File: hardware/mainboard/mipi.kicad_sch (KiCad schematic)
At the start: 41 parts

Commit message: More stuff
Signed-off-by: David Shah <dave@ds0.me>
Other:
- moved on the sheet: C?, FB?, U?J, U?K

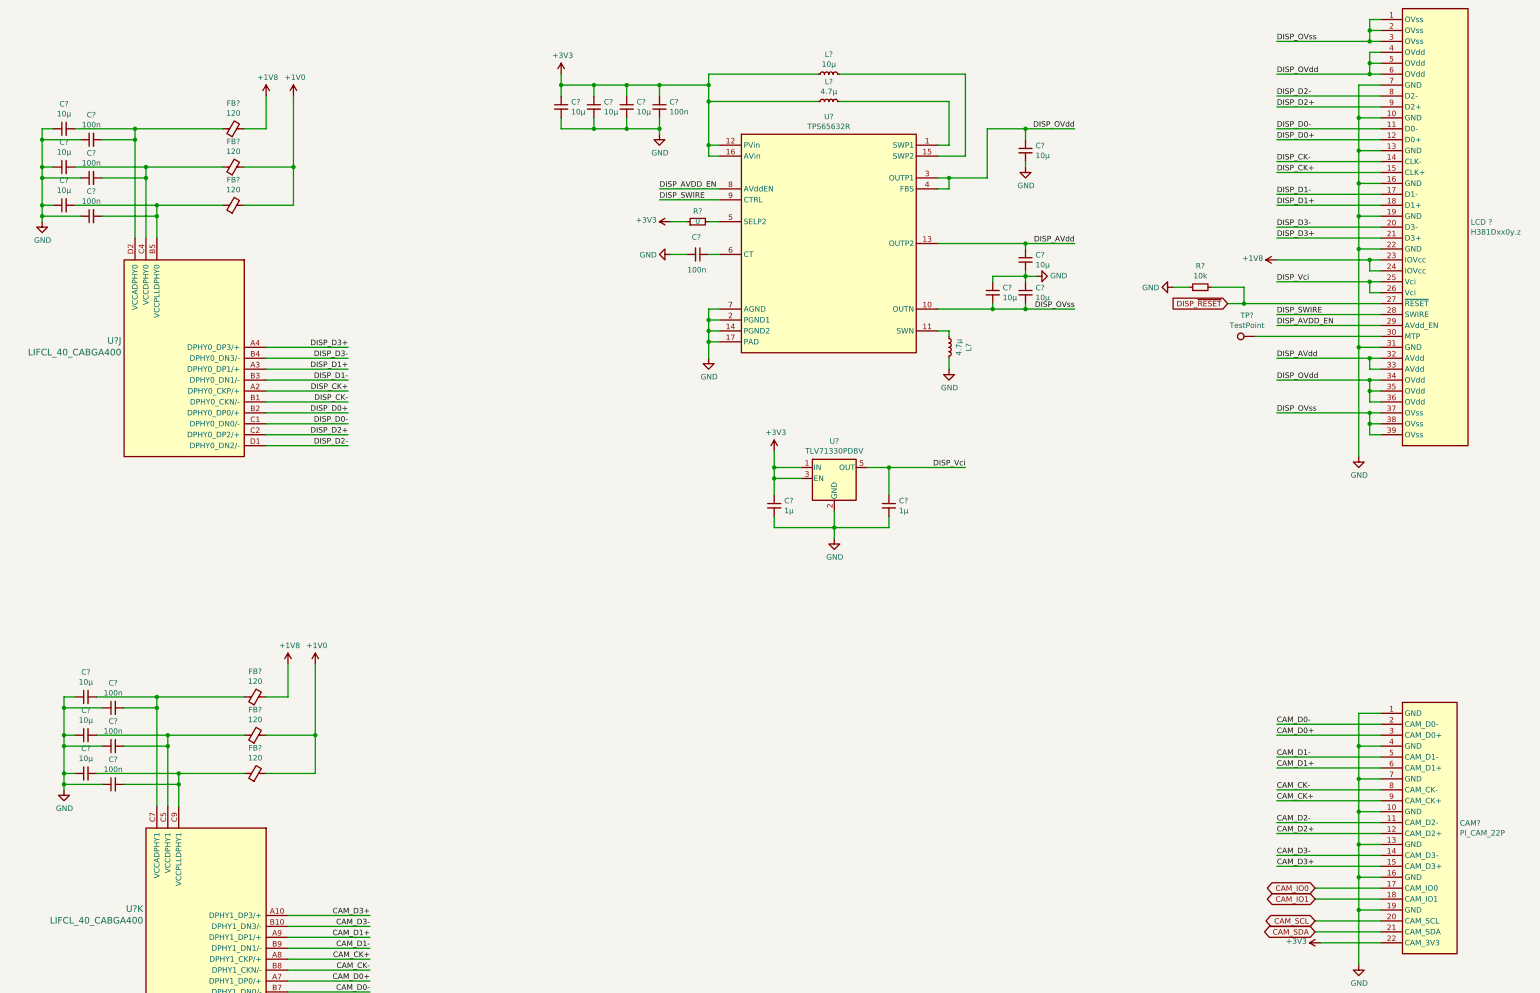
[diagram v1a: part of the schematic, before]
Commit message: Annotate and assign some footpints
Signed-off-by: David Shah <dave@ds0.me>
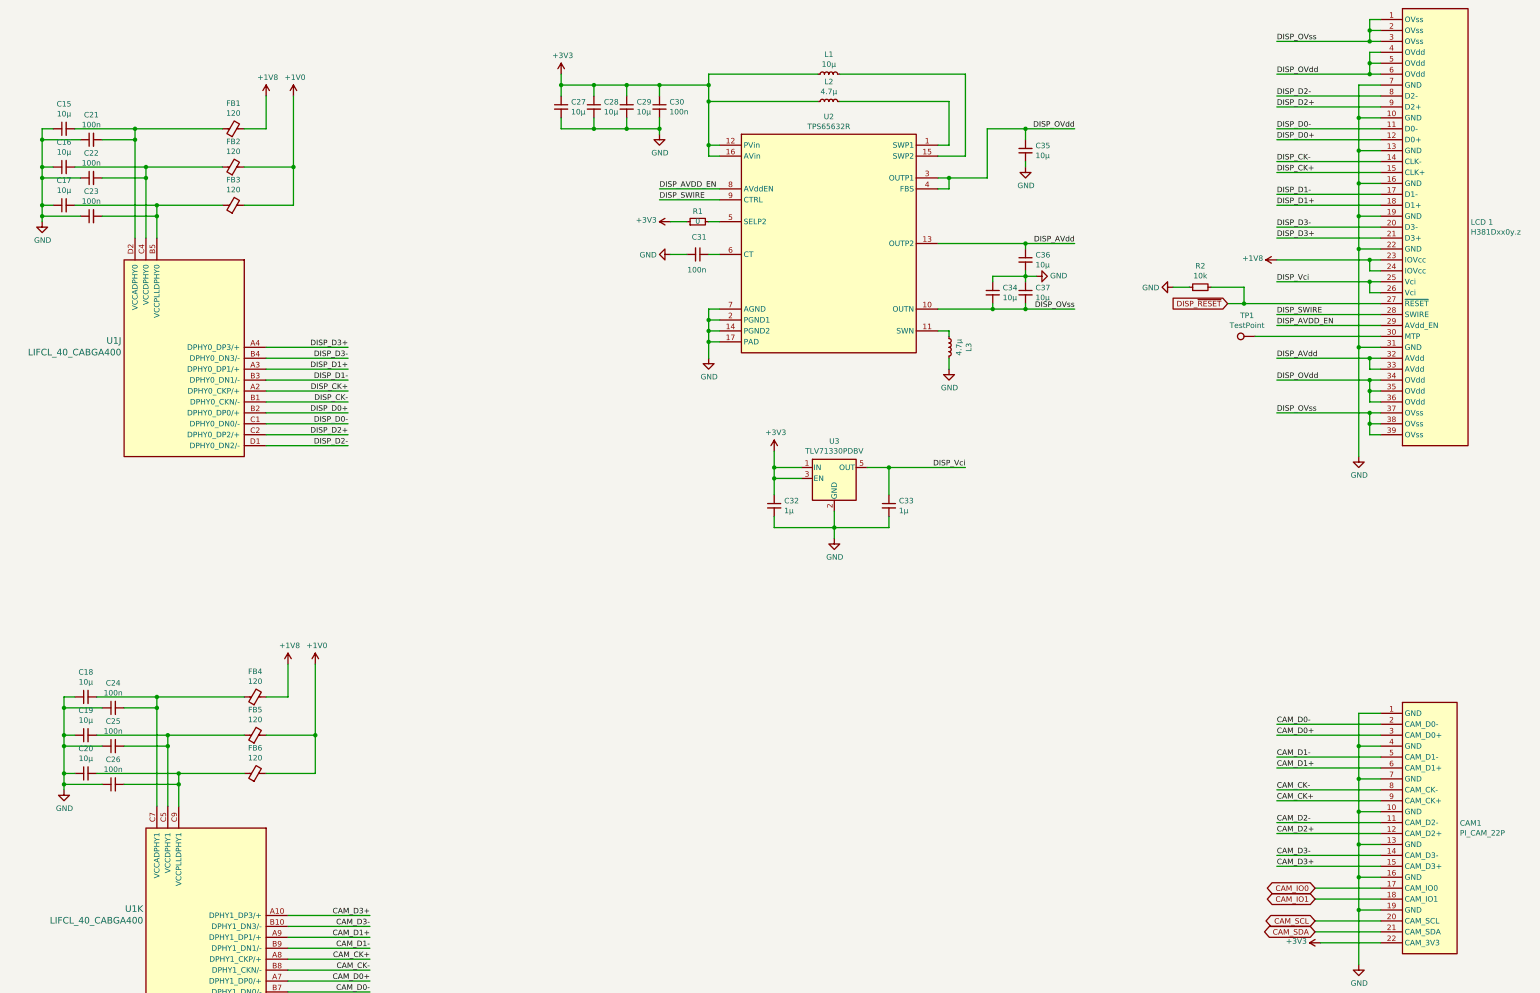
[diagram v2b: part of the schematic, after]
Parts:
- C15, C16, C17, C18, C19, C20, C27, C28, C29, C34, C35, C36, C37: renamed from C?; footprint (none) -> Capacitor_SMD:C_0805_2012Metric
- C21, C22, C23, C24, C25, C26, C30, C31: renamed from C?; footprint (none) -> Capacitor_SMD:C_0402_1005Metric
- C32, C33: renamed from C?; footprint (none) -> Capacitor_SMD:C_0603_1608Metric
- FB1, FB2, FB3, FB4, FB5, FB6: renamed from FB?; footprint (none) -> Inductor_SMD:L_0603_1608Metric
- LCD 1: renamed from LCD ?
- R1, R2: renamed from R?; footprint (none) -> Resistor_SMD:R_0402_1005Metric
- U2: renamed from U?; footprint (none) -> Package_DFN_QFN:QFN-16-1EP_3x3mm_P0.5mm_EP1.7x1.7mm
- gave numbers to parts that had none: 7

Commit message: Add and assign more footprints
Signed-off-by: David Shah <dave@ds0.me>
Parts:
- CAM1: footprint (none) -> meowality:54548-2271
- L1: value 10µ -> XFL3012-103MEB; footprint (none) -> meowality:XFL3012
- L2, L3: value 4.7µ -> XFL4020-472MEB; footprint (none) -> Inductor_SMD:L_Coilcraft_XxL4020
- LCD 1: footprint (none) -> meowality:FH35C-39S-0.3SHW
- TP1: footprint (none) -> TestPoint:TestPoint_Pad_D2.0mm
- U1: footprint (none) -> meowality:BGA-400_20x20_17.0x17.0mm
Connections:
- net GND: now also CAM1.M, LCD 1.M
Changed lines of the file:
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@@
   (junction (at 361.95 224.79) (diameter 1.016) (color 0 0 0 0))
   (junction (at 361.95 232.41) (diameter 1.016) (color 0 0 0 0))
+  (junction (at 361.95 242.57) (diameter 1.016) (color 0 0 0 0))
   (junction (at 364.49 27.94) (diameter 1.016) (color 0 0 0 0))
   (junction (at 364.49 30.48) (diameter 1.016) (color 0 0 0 0))
@@
     (stroke (width 0) (type solid) (color 0 0 0 0))
   )
-  (wire (pts (xy 361.95 232.41) (xy 361.95 245.11))
+  (wire (pts (xy 361.95 232.41) (xy 361.95 242.57))
     (stroke (width 0) (type solid) (color 0 0 0 0))
   )
@@
     (stroke (width 0) (type solid) (color 0 0 0 0))
   )
+  (wire (pts (xy 361.95 242.57) (xy 361.95 245.11))
+    (stroke (width 0) (type solid) (color 0 0 0 0))
+  )
+  (wire (pts (xy 361.95 242.57) (xy 367.03 242.57))
+    (stroke (width 0) (type solid) (color 0 0 0 0))
+  )
   (wire (pts (xy 364.49 25.4) (xy 364.49 27.94))
     (stroke (width 0) (type solid) (color 0 0 0 0))
@@
   )
   (wire (pts (xy 367.03 209.55) (xy 361.95 209.55))
+    (stroke (width 0) (type solid) (color 0 0 0 0))
+  )
+  (wire (pts (xy 397.51 121.92) (xy 392.43 121.92))
+    (stroke (width 0) (type solid) (color 0 0 0 0))
+  )
+  (wire (pts (xy 397.51 128.27) (xy 397.51 121.92))
     (stroke (width 0) (type solid) (color 0 0 0 0))
   )
@@
     (in_bom yes) (on_board yes)
     (property "Reference" "L1" (id 0) (at 238.76 33.5088 90))
-    (property "Value" "10µ" (id 1) (at 238.76 35.807 90))
-    (property "Footprint" "" (id 2) (at 238.76 38.1 0)
+    (property "Value" "XFL3012-103MEB" (id 1) (at 238.76 35.807 90))
+    (property "Footprint" "meowality:XFL3012" (id 2) (at 238.76 38.1 0)
       (effects (font (size 1.27 1.27)) hide)
     )
@@
     (in_bom yes) (on_board yes)
     (property "Reference" "L2" (id 0) (at 238.76 39.8588 90))
-    (property "Value" "4.7µ" (id 1) (at 238.76 42.157 90))
-    (property "Footprint" "" (id 2) (at 238.76 44.45 0)
+    (property "Value" "XFL4020-472MEB" (id 1) (at 238.76 42.157 90))
+    (property "Footprint" "Inductor_SMD:L_Coilcraft_XxL4020" (id 2) (at 238.76 44.45 0)
       (effects (font (size 1.27 1.27)) hide)
     )
@@
     (in_bom yes) (on_board yes)
     (property "Reference" "L3" (id 0) (at 271.2912 101.6 90))
-    (property "Value" "4.7µ" (id 1) (at 268.993 101.6 90))
-    (property "Footprint" "" (id 2) (at 266.7 101.6 0)
+    (property "Value" "XFL4020-472MEB" (id 1) (at 268.993 101.6 90))
+    (property "Footprint" "Inductor_SMD:L_Coilcraft_XxL4020" (id 2) (at 266.7 101.6 0)
       (effects (font (size 1.27 1.27)) hide)
     )
@@
     (property "Reference" "TP1" (id 0) (at 335.9785 94.2148 90))
     (property "Value" "TestPoint" (id 1) (at 335.9785 96.5135 90))
-    (property "Footprint" "" (id 2) (at 337.82 93.98 0)
+    (property "Footprint" "TestPoint:TestPoint_Pad_D2.0mm" (id 2) (at 337.82 93.98 0)
       (effects (font (size 1.27 1.27)) hide)
     )
@@
     )
     (property "Datasheet" "" (id 3) (at 361.95 245.11 0)
+      (effects (font (size 1.27 1.27)) hide)
+    )
+    (pin "1")
+  )
+  (symbol (lib_id "power:GND") (at 397.51 128.27 0) (unit 1)
+    (in_bom yes) (on_board yes)
+    (property "Reference" "#PWR0113" (id 0) (at 397.51 134.62 0)
+      (effects (font (size 1.27 1.27)) hide)
+    )
+    (property "Value" "GND" (id 1) (at 397.6243 132.5944 0))
+    (property "Footprint" "" (id 2) (at 397.51 128.27 0)
+      (effects (font (size 1.27 1.27)) hide)
+    )
+    (property "Datasheet" "" (id 3) (at 397.51 128.27 0)
       (effects (font (size 1.27 1.27)) hide)
     )
@@
     (pin "5")
   )
-  (symbol (lib_id "meowality:PI_CAM_22P") (at 378.46 242.57 0) (unit 1)
-    (in_bom yes) (on_board yes)
-    (property "Reference" "CAM1" (id 0) (at 385.4455 212.2106 0)
-      (effects (font (size 1.27 1.27)) (justify left))
-    )
-    (property "Value" "PI_CAM_22P" (id 1) (at 385.4455 214.5093 0)
-      (effects (font (size 1.27 1.27)) (justify left))
-    )
-    (property "Footprint" "" (id 2) (at 378.46 242.57 0)
-      (effects (font (size 1.27 1.27)) hide)
-    )
-    (property "Datasheet" "" (id 3) (at 378.46 242.57 0)
+  (symbol (lib_id "meowality:PI_CAM_22P") (at 378.46 245.11 0) (unit 1)
+    (in_bom yes) (on_board yes)
+    (property "Reference" "CAM1" (id 0) (at 385.4455 214.7506 0)
+      (effects (font (size 1.27 1.27)) (justify left))
+    )
+    (property "Value" "PI_CAM_22P" (id 1) (at 385.4455 217.0493 0)
+      (effects (font (size 1.27 1.27)) (justify left))
+    )
+    (property "Footprint" "meowality:54548-2271" (id 2) (at 378.46 245.11 0)
+      (effects (font (size 1.27 1.27)) hide)
+    )
+    (property "Datasheet" "" (id 3) (at 378.46 245.11 0)
       (effects (font (size 1.27 1.27)) hide)
     )
@@
     (pin "21")
     (pin "22")
+    (pin "M")
   )
   (symbol (lib_id "meowality:LIFCL_40_CABGA400") (at 107.95 101.6 0) (mirror y) (unit 10)
@@
       (effects (font (size 1.524 1.524)) (justify left))
     )
-    (property "Footprint" "" (id 2) (at 104.14 100.33 0)
+    (property "Footprint" "meowality:BGA-400_20x20_17.0x17.0mm" (id 2) (at 104.14 100.33 0)
       (effects (font (size 1.524 1.524)) (justify right) hide)
     )
@@
       (effects (font (size 1.524 1.524)) (justify left))
     )
-    (property "Footprint" "" (id 2) (at 109.22 232.41 0)
+    (property "Footprint" "meowality:BGA-400_20x20_17.0x17.0mm" (id 2) (at 109.22 232.41 0)
       (effects (font (size 1.524 1.524)) (justify right) hide)
     )
@@
     (pin "B6")
   )
+  (symbol (lib_id "meowality:TPS65632R") (at 238.76 77.47 0) (unit 1)
+    (in_bom yes) (on_board yes)
+    (property "Reference" "U2" (id 0) (at 238.76 47.9863 0))
+    (property "Value" "TPS65632R" (id 1) (at 238.76 50.285 0))
+    (property "Footprint" "Package_DFN_QFN:QFN-16-1EP_3x3mm_P0.5mm_EP1.7x1.7mm" (id 2) (at 238.76 92.71 0)
+      (effects (font (size 1.27 1.27)) hide)
+    )
+    (property "Datasheet" "" (id 3) (at 238.76 92.71 0)
+      (effects (font (size 1.27 1.27)) hide)
+    )
+    (pin "12")
+    (pin "16")
+    (pin "8")
+    (pin "9")
+    (pin "5")
+    (pin "6")
+    (pin "7")
+    (pin "2")
+    (pin "14")
+    (pin "17")
+    (pin "1")
+    (pin "15")
+    (pin "3")
+    (pin "4")
+    (pin "13")
+    (pin "10")
+    (pin "11")
+  )
   (symbol (lib_id "meowality:H381Dxx0y.z") (at 379.73 73.66 0) (unit 1)
     (in_bom yes) (on_board yes)
@@
       (effects (font (size 1.27 1.27)) (justify left))
     )
-    (property "Footprint" "" (id 2) (at 382.27 127 0)
+    (property "Footprint" "meowality:FH35C-39S-0.3SHW" (id 2) (at 382.27 127 0)
       (effects (font (size 1.27 1.27)) hide)
     )
@@
     (pin "38")
     (pin "39")
-  )
-  (symbol (lib_id "meowality:TPS65632R") (at 238.76 77.47 0) (unit 1)
-    (in_bom yes) (on_board yes)
-    (property "Reference" "U2" (id 0) (at 238.76 47.9863 0))
-    (property "Value" "TPS65632R" (id 1) (at 238.76 50.285 0))
-    (property "Footprint" "Package_DFN_QFN:QFN-16-1EP_3x3mm_P0.5mm_EP1.7x1.7mm" (id 2) (at 238.76 92.71 0)
-      (effects (font (size 1.27 1.27)) hide)
-    )
-    (property "Datasheet" "" (id 3) (at 238.76 92.71 0)
-      (effects (font (size 1.27 1.27)) hide)
-    )
-    (pin "12")
-    (pin "16")
-    (pin "8")
-    (pin "9")
-    (pin "5")
-    (pin "6")
-    (pin "7")
-    (pin "2")
-    (pin "14")
-    (pin "17")
-    (pin "1")
-    (pin "15")
-    (pin "3")
-    (pin "4")
-    (pin "13")
-    (pin "10")
-    (pin "11")
+    (pin "M")
   )
 )

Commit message: First pass at placement
Signed-off-by: David Shah <dave@ds0.me>
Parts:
- LCD1: renamed from LCD 1
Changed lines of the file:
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@@
   (symbol (lib_id "meowality:H381Dxx0y.z") (at 379.73 73.66 0) (unit 1)
     (in_bom yes) (on_board yes)
-    (property "Reference" "LCD\n1" (id 0) (at 387.9855 72.5106 0)
+    (property "Reference" "LCD1" (id 0) (at 387.9855 72.5106 0)
       (effects (font (size 1.27 1.27)) (justify left))
     )

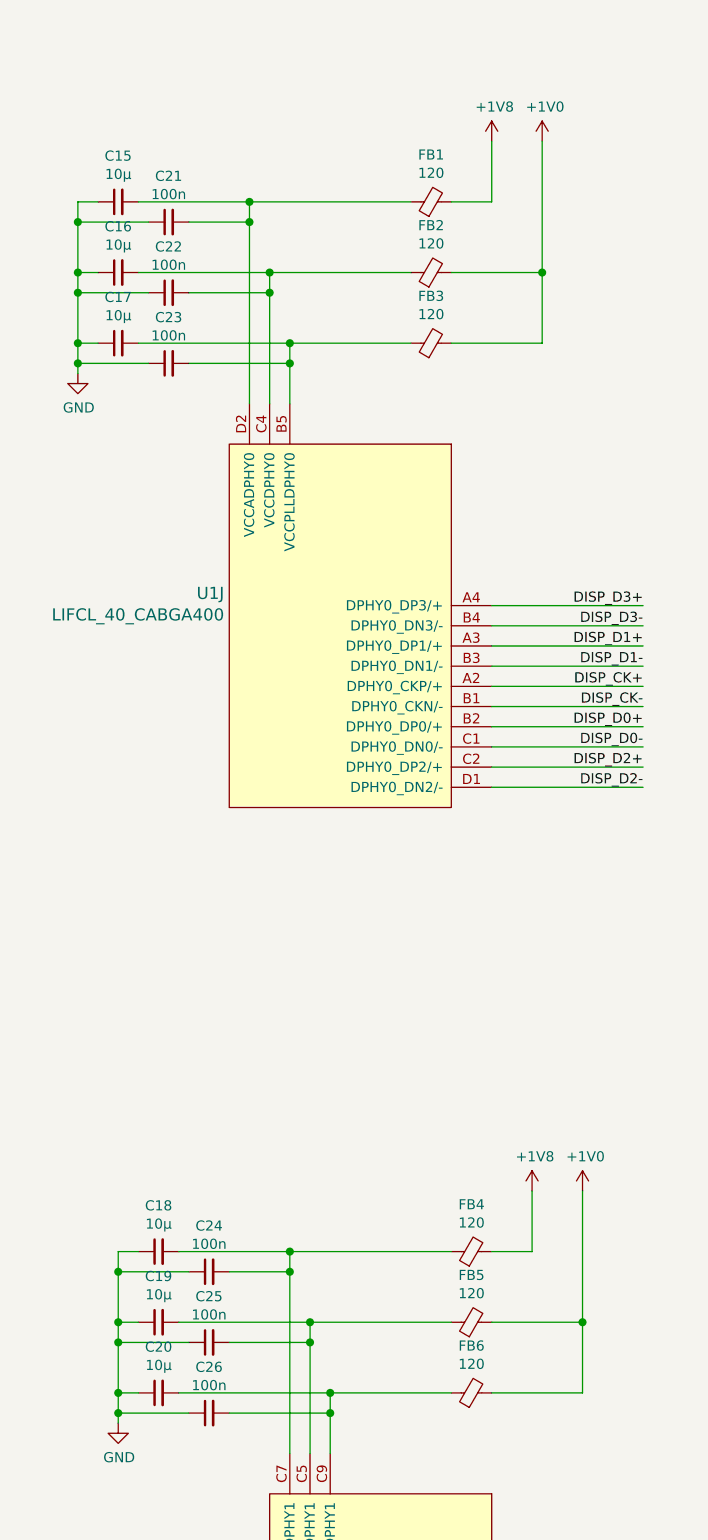
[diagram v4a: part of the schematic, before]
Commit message: mainboard: Fix some schematic ERC issues
Signed-off-by: gatecat <gatecat@ds0.me>
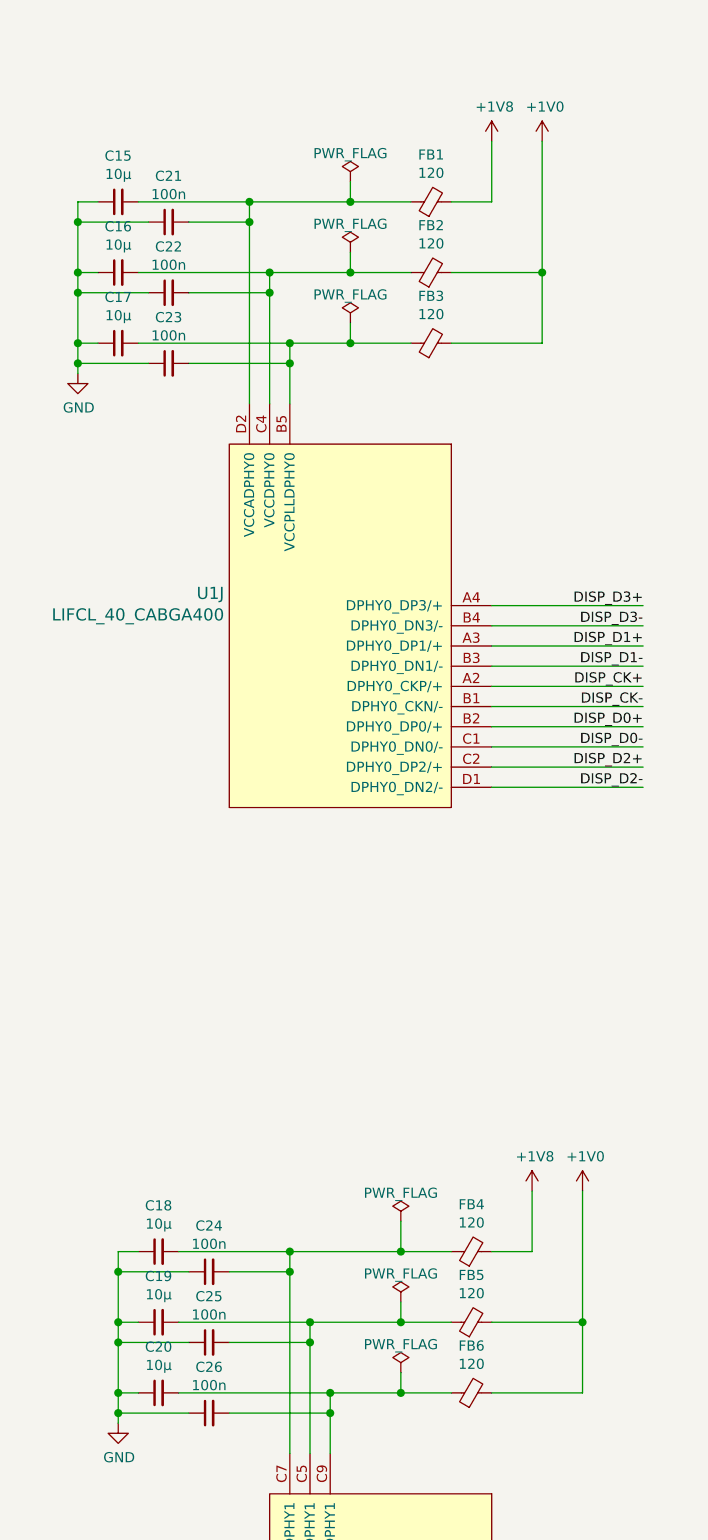
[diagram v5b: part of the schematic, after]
